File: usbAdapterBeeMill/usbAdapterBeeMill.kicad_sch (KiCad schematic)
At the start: 2 parts, among them J1 Conn_02x05_Odd_Even, J2 USB_A

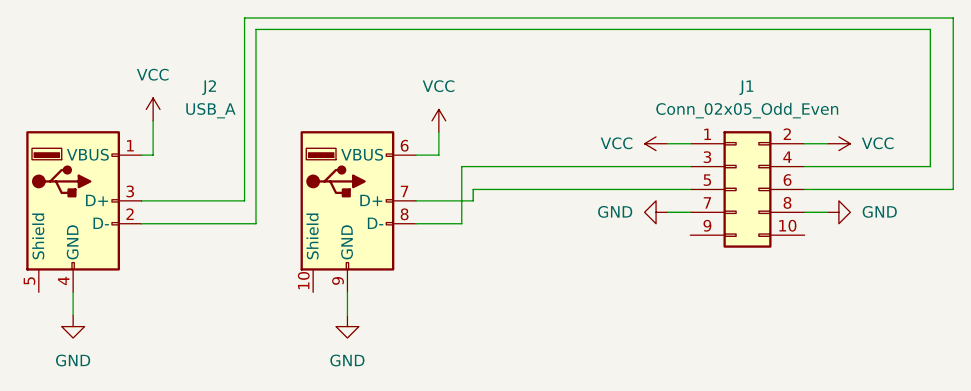
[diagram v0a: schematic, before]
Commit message: change D+ and D-
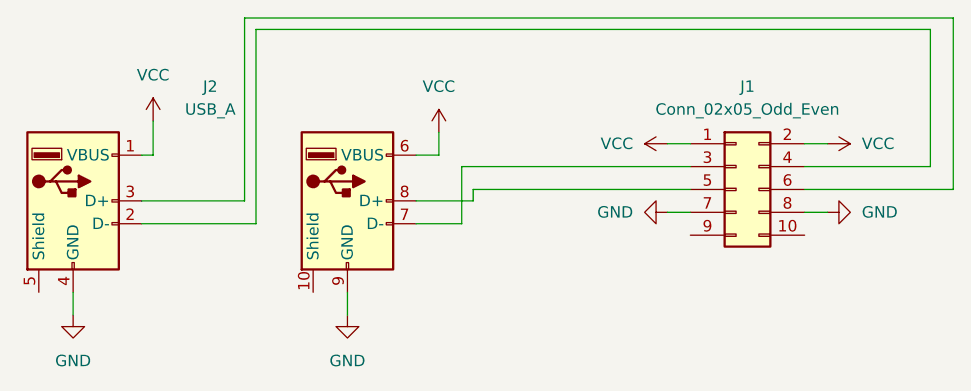
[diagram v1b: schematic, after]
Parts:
- J2: footprint usbAdapter:usbDouble -> (none)
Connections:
- net at J1.3 (Pin_3): now also J2.7 (D-); no longer J2.8 (D-)
- net at J1.5 (Pin_5): now also J2.8 (D+); no longer J2.7 (D+)
